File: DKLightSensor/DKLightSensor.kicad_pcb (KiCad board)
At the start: 2 copper layers, 9 parts, among them J1 Conn_01x03, U1 LMC6482

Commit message: Continued layout
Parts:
- moved J1 41.2 mm to (62.0, 35.1)
- moved U1 31.4 mm to (50.8, 33.7)
- moved RV1 28.7 mm to (68.0, 34.6), turned to 180 degrees
- moved C1 19.4 mm to (47.0, 43.4), turned to 180 degrees
- moved R1 16.6 mm to (44.2, 40.6), turned to 90 degrees
- moved R2 15.9 mm to (47.0, 38.1), turned to -90 degrees
- moved C2 15.5 mm to (48.3, 33.8), turned to 90 degrees
- moved R3 14.2 mm to (42.9, 33.3), turned to -90 degrees
- moved D1 5.33 mm to (37.6, 36.6), turned to 90 degrees
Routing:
- net +3.3V: track 0.00 -> 9.31 mm
- net Net-(D1-A): track 0.00 -> 6.09 mm

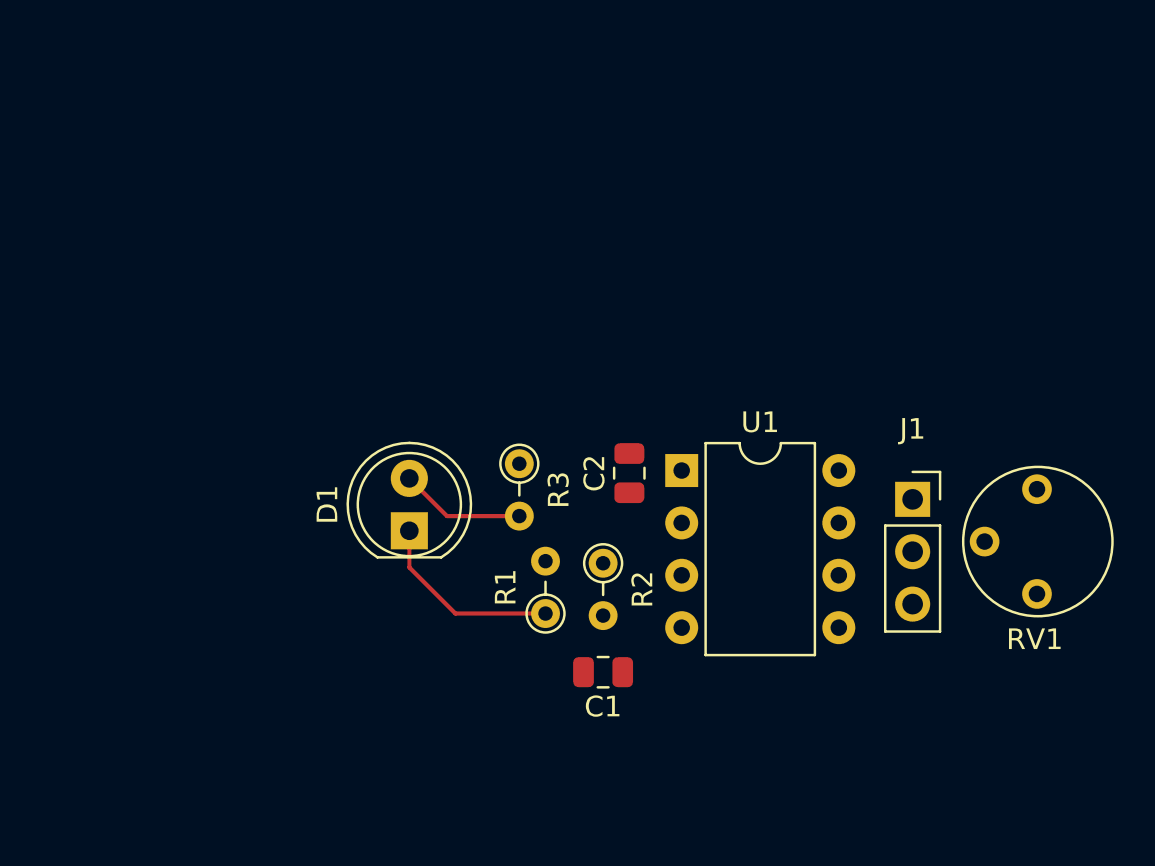
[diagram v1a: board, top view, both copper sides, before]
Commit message: Changed connector placement
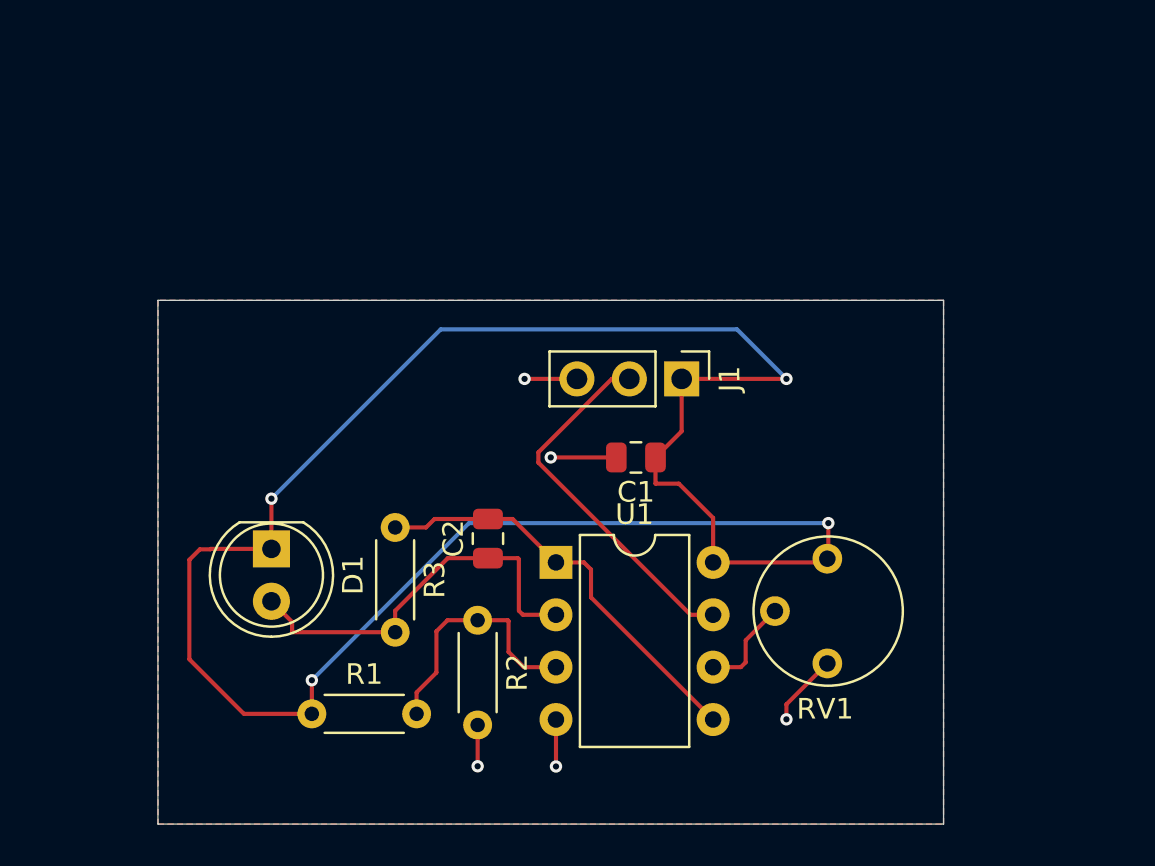
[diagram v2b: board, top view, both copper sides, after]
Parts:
- J1: footprint Connector_PinSocket_2.54mm:PinSocket_1x03_P2.54mm_Vertical -> Connector_PinHeader_2.54mm:PinHeader_1x03_P2.54mm_Vertical
- R1, R2, R3: footprint Resistor_THT:R_Axial_DIN0204_L3.6mm_D1.6mm_P2.54mm_Vertical -> Resistor_THT:R_Axial_DIN0204_L3.6mm_D1.6mm_P5.08mm_Horizontal
- moved J1 12.6 mm to (50.8, 29.2), turned to -90 degrees
- moved R1 12.3 mm to (32.9, 45.5), turned to 0 degrees
- moved RV1 10.7 mm to (57.9, 37.9)
- moved C1 10.5 mm to (48.6, 33.0)
- moved C2 7.55 mm to (41.4, 37.0)
- moved U1 7.55 mm to (44.7, 38.1)
- moved R3 6.77 mm to (36.9, 36.4)
- moved D1 6.75 mm to (30.9, 37.5), turned to -90 degrees
- moved R2 6.68 mm to (40.9, 40.9)
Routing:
- net +3.3V: track 9.31 -> 101.4 mm, vias 0 -> 4
- net Net-(U1B-+): track 0.00 -> 20.4 mm
- net Net-(J1-Pin_2): track 0.00 -> 17.9 mm
- net GND: track 0.00 -> 13.5 mm, vias 0 -> 5
- net Net-(D1-A): track 6.09 -> 19.4 mm
- net Net-(U1A-+): track 0.00 -> 12.2 mm
- net Net-(U1B--): track 0.00 -> 4.75 mm
- added copper zone on B.Cu, net GND
- added copper zone on F.Cu, net GND
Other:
- board outline added: 38.1 x 25.4 mm

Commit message: minimized daisy-chaining (tried to route directly from input power source)
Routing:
- net +3.3V: track 101.4 -> 119.3 mm
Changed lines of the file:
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@@
 		(tags "Resistor Axial_DIN0204 series Axial Horizontal pin pitch 5.08mm 0.167W length 3.6mm diameter 1.6mm")
 		(property "Reference" "R1"
-			(at 2.54 -1.92 360)
+			(at 2.54 -1.92 0)
 			(layer "F.SilkS")
 			(effects
@@
 		)
 		(property "Value" "10k"
-			(at 2.54 1.92 360)
+			(at 2.54 1.92 0)
 			(layer "F.Fab")
 			(effects
@@
 		)
 		(fp_text user "${REFERENCE}"
-			(at 2.54 0 360)
+			(at 2.54 0 0)
 			(layer "F.Fab")
 			(effects
@@
 		)
 		(fp_text user "${REFERENCE}"
-			(at 0 2.54 360)
+			(at 0 2.54 0)
 			(layer "F.Fab")
 			(effects
@@
 		(tags "capacitor")
 		(property "Reference" "C1"
-			(at 0 -1.68 360)
+			(at 0 -1.68 0)
 			(layer "F.SilkS")
 			(effects
@@
 		)
 		(property "Value" "1uF"
-			(at 0 1.68 360)
+			(at 0 1.68 0)
 			(layer "F.Fab")
 			(effects
@@
 		)
 		(fp_text user "${REFERENCE}"
-			(at 0 0 360)
+			(at 0 0 0)
 			(layer "F.Fab")
 			(effects
@@
 	)
 	(segment
-		(start 49.53 34.29)
-		(end 50.659 34.29)
-		(width 0.2)
-		(layer "F.Cu")
-		(net 1)
-	)
-	(segment
 		(start 50.8 31.75)
 		(end 50.8 29.21)
@@
 	)
 	(segment
-		(start 57.912 36.205)
-		(end 57.912 37.881)
+		(start 50.8 29.21)
+		(end 52.07 30.48)
 		(width 0.2)
 		(layer "F.Cu")
@@
 	)
 	(segment
+		(start 57.863 37.93)
+		(end 57.863 36.273)
+		(width 0.2)
+		(layer "F.Cu")
+		(net 1)
+	)
+	(segment
 		(start 27.94 37.475)
 		(end 27.96 37.455)
@@
 	)
 	(segment
-		(start 49.53 33.02)
-		(end 49.53 34.29)
-		(width 0.2)
-		(layer "F.Cu")
-		(net 1)
-	)
-	(segment
 		(start 29.57 45.455)
 		(end 26.924 42.809)
@@
 	)
 	(segment
+		(start 52.07 37.856)
+		(end 52.324 38.11)
+		(width 0.2)
+		(layer "F.Cu")
+		(net 1)
+	)
+	(segment
 		(start 32.864 45.455)
 		(end 29.57 45.455)
@@
 	)
 	(segment
-		(start 50.659 34.29)
-		(end 52.324 35.955)
+		(start 57.863 36.273)
+		(end 50.8 29.21)
 		(width 0.2)
 		(layer "F.Cu")
@@
 	)
 	(segment
-		(start 52.324 35.955)
-		(end 52.324 38.11)
+		(start 54.61 33.02)
+		(end 54.61 36.205)
+		(width 0.2)
+		(layer "F.Cu")
+		(net 1)
+	)
+	(segment
+		(start 50.8 29.21)
+		(end 54.61 33.02)
+		(width 0.2)
+		(layer "F.Cu")
+		(net 1)
+	)
+	(segment
+		(start 52.07 30.48)
+		(end 52.07 37.856)
 		(width 0.2)
 		(layer "F.Cu")
@@
 	)
 	(via
-		(at 57.912 36.205)
+		(at 54.61 36.205)
 		(size 0.6)
 		(drill 0.3)
@@
 	)
 	(segment
-		(start 40.484 36.205)
-		(end 57.912 36.205)
-		(width 0.2)
-		(layer "B.Cu")
-		(net 1)
-	)
-	(segment
 		(start 53.477 26.807)
 		(end 39.116 26.807)
@@
 	)
 	(segment
+		(start 40.484 36.205)
+		(end 32.864 43.825)
+		(width 0.2)
+		(layer "B.Cu")
+		(net 1)
+	)
+	(segment
 		(start 55.88 29.21)
 		(end 53.477 26.807)
@@
 	)
 	(segment
-		(start 32.864 43.825)
+		(start 54.61 36.205)
 		(end 40.484 36.205)
 		(width 0.2)

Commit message: deleted trace between diode and resistor
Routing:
- net +3.3V: track 119.3 -> 103.2 mm
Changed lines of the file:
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@@
-	)
-	(segment
-		(start 27.96 37.455)
-		(end 30.904 37.455)
-		(width 0.2)
-		(layer "F.Cu")
-		(net 1)
 	)
 	(segment
@@
 	)
 	(segment
-		(start 27.94 37.475)
-		(end 27.96 37.455)
-		(width 0.2)
-		(layer "F.Cu")
-		(net 1)
-	)
-	(segment
-		(start 29.57 45.455)
-		(end 26.924 42.809)
-		(width 0.2)
-		(layer "F.Cu")
-		(net 1)
-	)
-	(segment
 		(start 52.07 37.856)
 		(end 52.324 38.11)
-		(width 0.2)
-		(layer "F.Cu")
-		(net 1)
-	)
-	(segment
-		(start 32.864 45.455)
-		(end 29.57 45.455)
 		(width 0.2)
 		(layer "F.Cu")
@@
 	)
 	(segment
-		(start 26.924 42.809)
-		(end 26.924 37.983)
-		(width 0.2)
-		(layer "F.Cu")
-		(net 1)
-	)
-	(segment
 		(start 32.864 43.825)
 		(end 32.864 45.455)
@@
 		(width 0.2)
 		(layer "F.Cu")
-		(net 1)
-	)
-	(segment
-		(start 26.924 37.983)
-		(end 27.432 37.475)
-		(width 0.2)
-		(layer "F.Cu")
-		(net 1)
-	)
-	(segment
-		(start 27.432 37.475)
-		(end 27.94 37.475)
-		(width 0.2)
-		(layer "F.Cu")

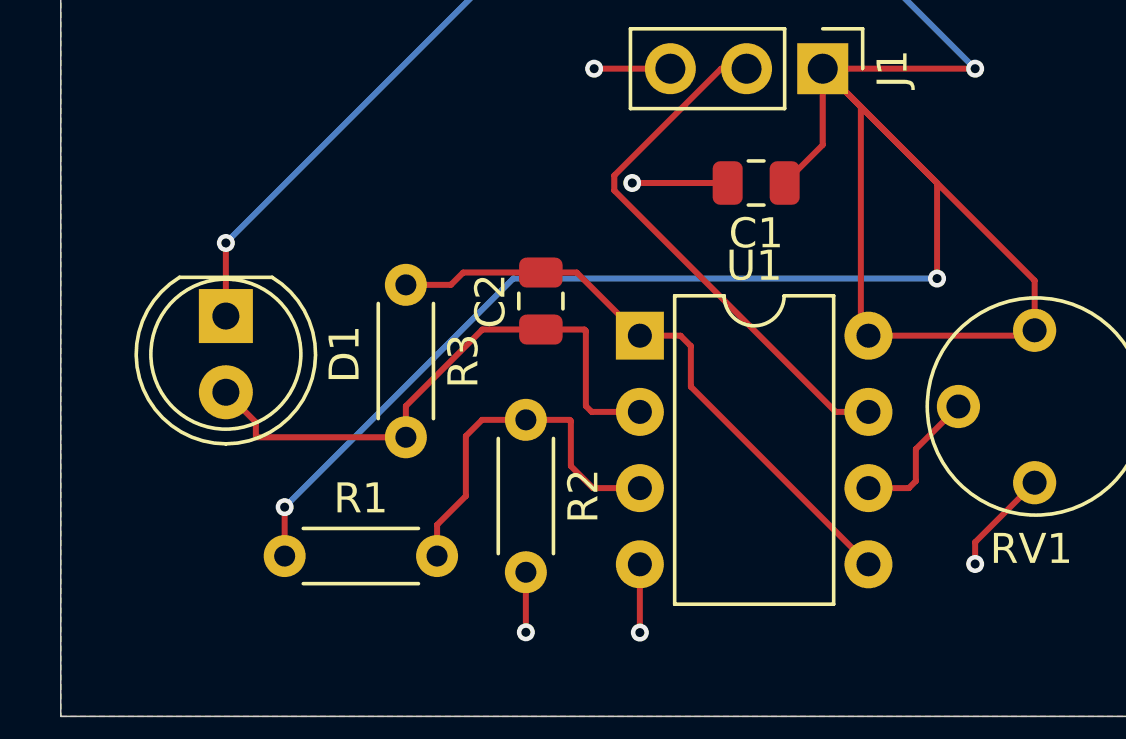
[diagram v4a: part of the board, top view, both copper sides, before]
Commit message: finished usb charger schematic
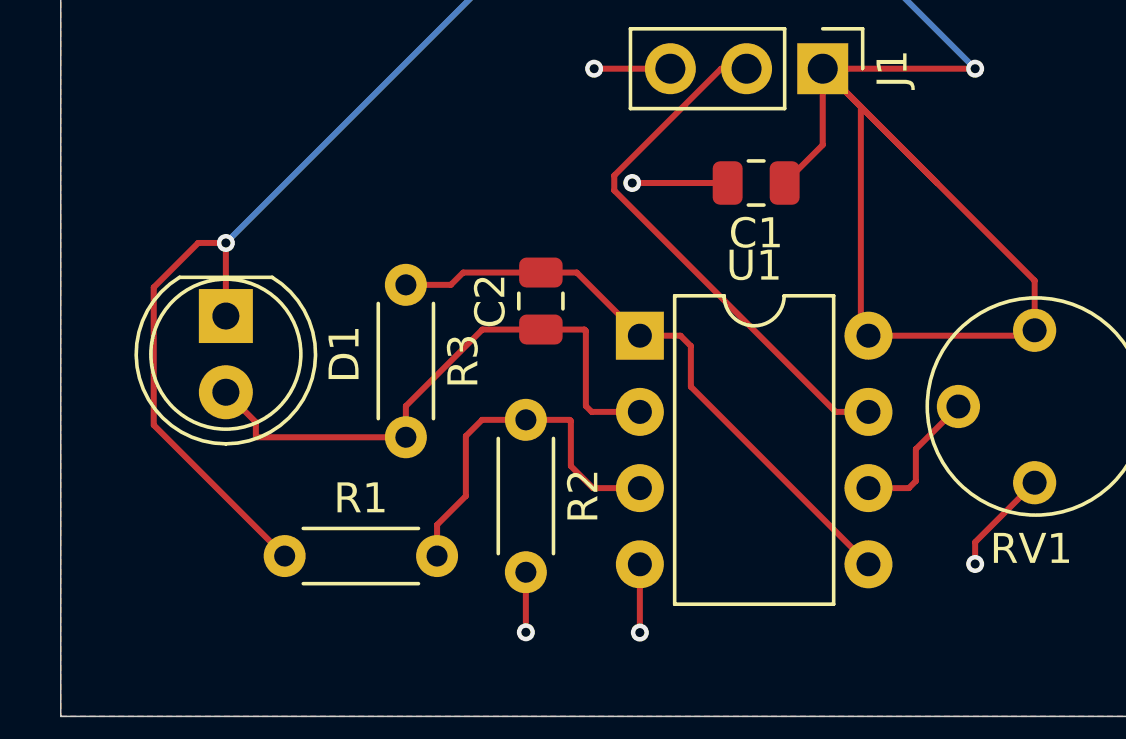
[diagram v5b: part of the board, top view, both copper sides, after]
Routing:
- net +3.3V: track 103.2 -> 87.3 mm, vias 4 -> 2
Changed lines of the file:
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@@
+	)
+	(segment
+		(start 29.981 35.019)
+		(end 28.5 36.5)
+		(width 0.2)
+		(layer "F.Cu")
+		(net 1)
 	)
 	(segment
@@
 		(start 30.904 35.019)
 		(end 30.904 37.455)
+		(width 0.2)
+		(layer "F.Cu")
+		(net 1)
+	)
+	(segment
+		(start 30.904 35.019)
+		(end 29.981 35.019)
 		(width 0.2)
 		(layer "F.Cu")
@@
 	)
 	(segment
-		(start 32.864 43.825)
-		(end 32.864 45.455)
+		(start 57.683 38.11)
+		(end 57.863 37.93)
 		(width 0.2)
 		(layer "F.Cu")
@@
 	)
 	(segment
-		(start 57.683 38.11)
-		(end 57.863 37.93)
+		(start 28.5 36.5)
+		(end 28.5 41.091)
+		(width 0.2)
+		(layer "F.Cu")
+		(net 1)
+	)
+	(segment
+		(start 28.5 41.091)
+		(end 32.864 45.455)
 		(width 0.2)
 		(layer "F.Cu")
@@
 		(start 52.324 38.11)
 		(end 57.683 38.11)
-		(width 0.2)
-		(layer "F.Cu")
-		(net 1)
-	)
-	(segment
-		(start 54.61 33.02)
-		(end 54.61 36.205)
 		(width 0.2)
 		(layer "F.Cu")
@@
 	)
 	(via
-		(at 54.61 36.205)
-		(size 0.6)
-		(drill 0.3)
-		(layers "F.Cu" "B.Cu")
-		(free yes)
-		(net 1)
-	)
-	(via
 		(at 55.88 29.21)
-		(size 0.6)
-		(drill 0.3)
-		(layers "F.Cu" "B.Cu")
-		(free yes)
-		(net 1)
-	)
-	(via
-		(at 32.864 43.825)
 		(size 0.6)
 		(drill 0.3)
@@
 	)
 	(segment
-		(start 40.484 36.205)
-		(end 32.864 43.825)
-		(width 0.2)
-		(layer "B.Cu")
-		(net 1)
-	)
-	(segment
 		(start 55.88 29.21)
 		(end 53.477 26.807)
 		(width 0.2)
 		(layer "B.Cu")
-		(net 1)
-	)
-	(segment
-		(start 54.61 36.205)
-		(end 40.484 36.205)
-		(width 0.2)
-		(layer "B.Cu")
